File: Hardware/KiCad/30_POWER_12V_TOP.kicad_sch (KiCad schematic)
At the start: 0 parts

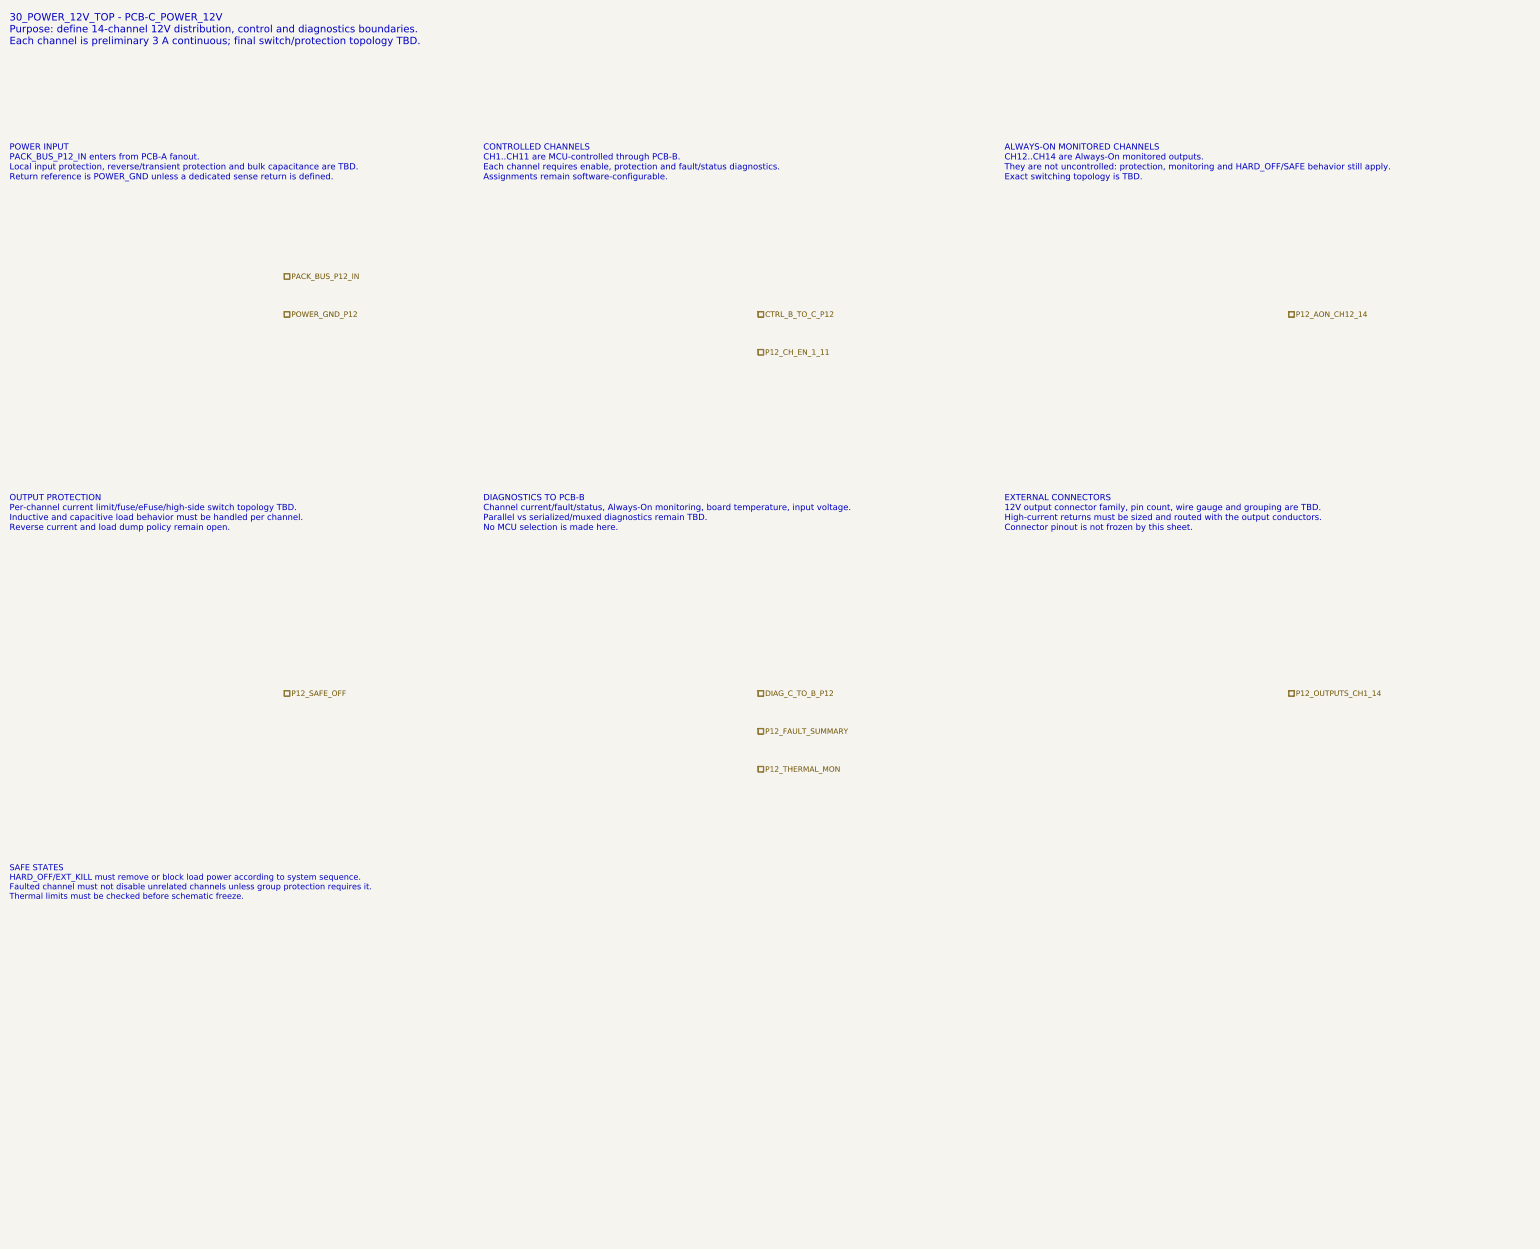
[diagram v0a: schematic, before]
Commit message: hardware: map PCB-C POWER_12V detailed hierarchy
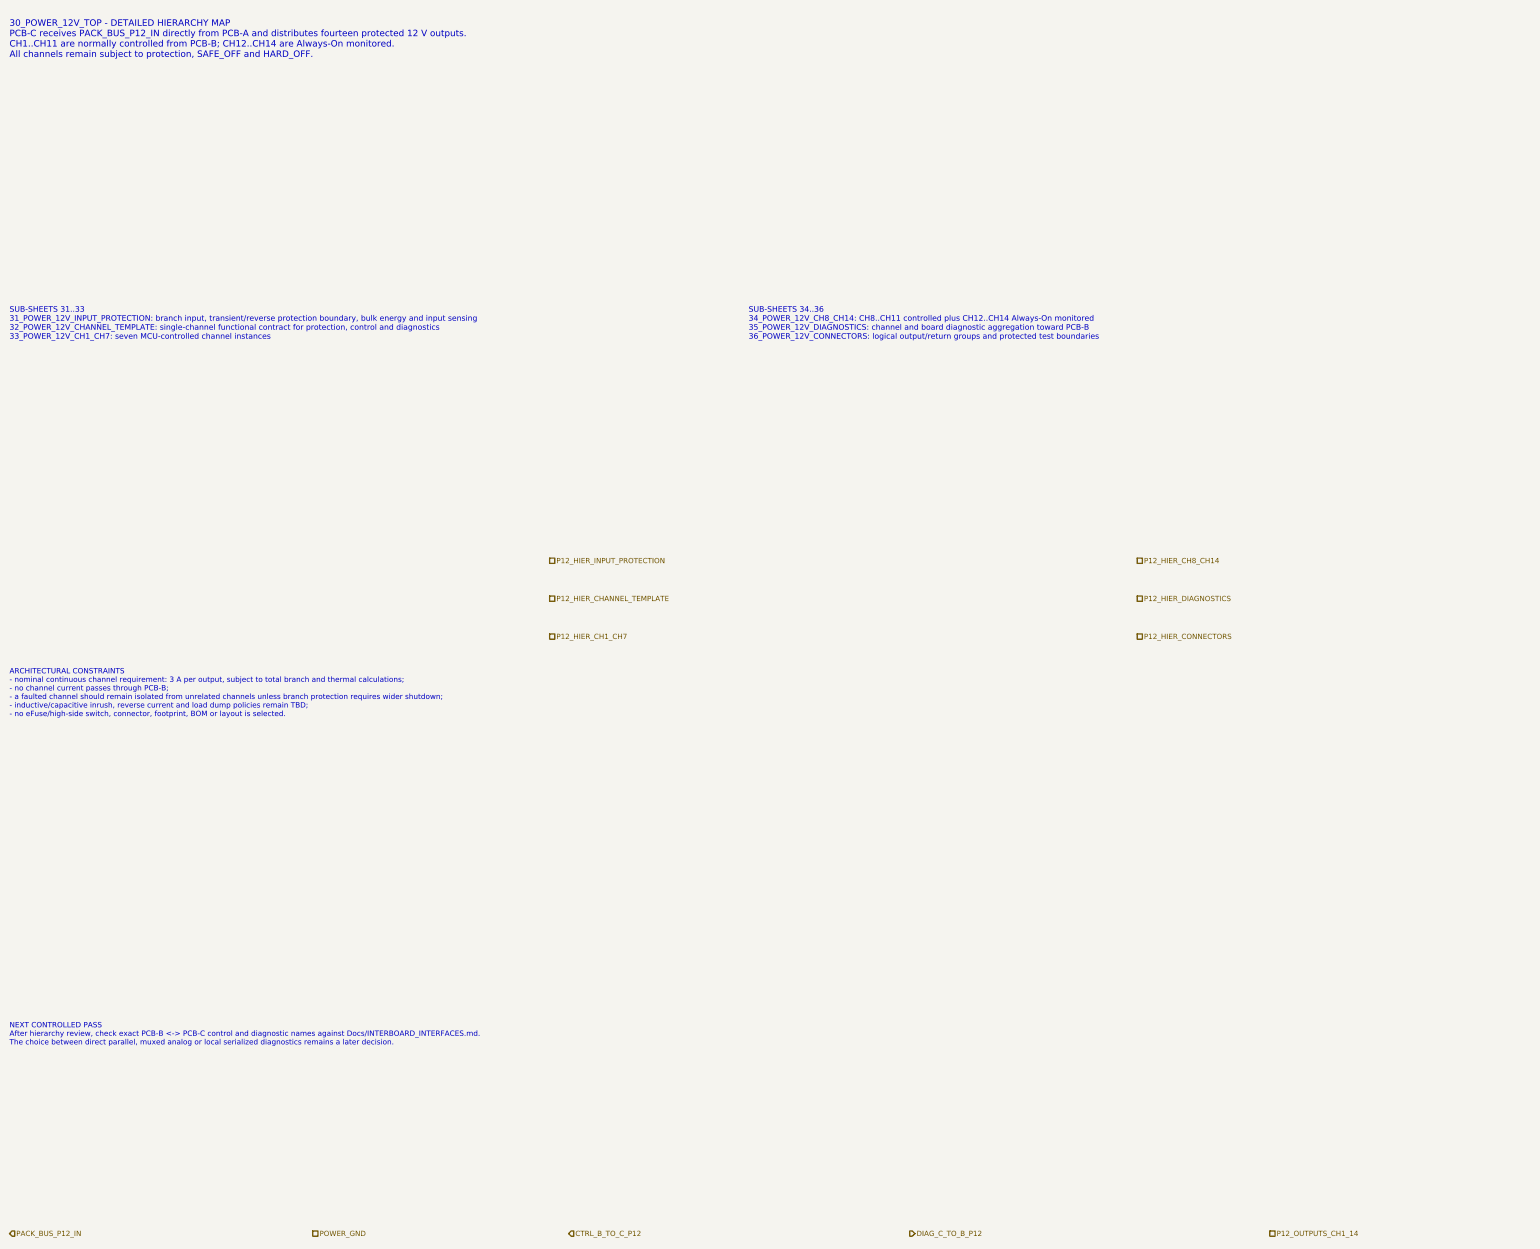
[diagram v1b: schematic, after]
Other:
- note added: "30_POWER_12V_TOP - DETAILED HIERARCHY MAP PCB-C receives PACK_BUS_P12_IN directly from PCB-A and distributes fourteen protected 12 V outputs. CH1..CH11 are normally controlled from PCB-B; CH12..CH14 are Always-On monitored. All channels remain subject to protection, SAFE_OFF and HARD_OFF."
- note added: "ARCHITECTURAL CONSTRAINTS - nominal continuous channel requirement: 3 A per output, subject to total branch and thermal calculations; - no channel current passes through PCB-B; - a faulted channel should remain isolated from unrelated channels unless branch protection requires wider shutdown; - inductive/capacitive inrush, reverse current and load dump policies remain TBD; - no eFuse/high-side sw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"
- note added: "NEXT CONTROLLED PASS After hierarchy review, check exact PCB-B <-> PCB-C control and diagnostic names against Docs/INTERBOARD_INTERFACES.md. The choice between direct parallel, muxed analog or local serialized diagnostics remains a later decision."
- note added: "SUB-SHEETS 31..33 31_POWER_12V_INPUT_PROTECTION: branch input, transient/reverse protection boundary, bulk energy and input sensing 32_POWER_12V_CHANNEL_TEMPLATE: single-channel functional contract for protection, control and diagnostics 33_POWER_12V_CH1_CH7: seven MCU-controlled channel instances"
- note added: "SUB-SHEETS 34..36 34_POWER_12V_CH8_CH14: CH8..CH11 controlled plus CH12..CH14 Always-On monitored 35_POWER_12V_DIAGNOSTICS: channel and board diagnostic aggregation toward PCB-B 36_POWER_12V_CONNECTORS: logical output/return groups and protected test boundaries"
- note removed: "30_POWER_12V_TOP - PCB-C_POWER_12V Purpose: define 14-channel 12V distribution, control and diagnostics boundaries. Each channel is preliminary 3 A continuous; final switch/protection topology TBD."
- note removed: "ALWAYS-ON MONITORED CHANNELS CH12..CH14 are Always-On monitored outputs. They are not uncontrolled: protection, monitoring and HARD_OFF/SAFE behavior still apply. Exact switching topology is TBD."
- note removed: "CONTROLLED CHANNELS CH1..CH11 are MCU-controlled through PCB-B. Each channel requires enable, protection and fault/status diagnostics. Assignments remain software-configurable."
- note removed: "DIAGNOSTICS TO PCB-B Channel current/fault/status, Always-On monitoring, board temperature, input voltage. Parallel vs serialized/muxed diagnostics remain TBD. No MCU selection is made here."
- note removed: "EXTERNAL CONNECTORS 12V output connector family, pin count, wire gauge and grouping are TBD. High-current returns must be sized and routed with the output conductors. Connector pinout is not frozen by this sheet."
- note removed: "OUTPUT PROTECTION Per-channel current limit/fuse/eFuse/high-side switch topology TBD. Inductive and capacitive load behavior must be handled per channel. Reverse current and load dump policy remain open."
- note removed: "POWER INPUT PACK_BUS_P12_IN enters from PCB-A fanout. Local input protection, reverse/transient protection and bulk capacitance are TBD. Return reference is POWER_GND unless a dedicated sense return is defined."
- note removed: "SAFE STATES HARD_OFF/EXT_KILL must remove or block load power according to system sequence. Faulted channel must not disable unrelated channels unless group protection requires it. Thermal limits must be checked before schematic freeze."
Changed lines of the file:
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@@
 		(title "30_POWER_12V_TOP - PCB-C_POWER_12V")
 		(date "2026-07-15")
-		(rev "A1")
+		(rev "A2")
 		(company "Gonoboben/plataVM")
-		(comment 1 "Architecture Level A: 14-channel 12V distribution")
-		(comment 2 "No eFuse/high-side switch part numbers or footprints selected")
+		(comment 1 "Architecture Level A/B: 14-channel POWER_12V detailed hierarchy map")
+		(comment 2 "Sub-sheets 31..36 define functional boundaries only; no components selected")
 	)
-	(text "30_POWER_12V_TOP - PCB-C_POWER_12V\nPurpose: define 14-channel 12V distribution, control and diagnostics boundaries.\nEach channel is preliminary 3 A continuous; final switch/protection topology TBD."
+	(text "30_POWER_12V_TOP - DETAILED HIERARCHY MAP\nPCB-C receives PACK_BUS_P12_IN directly from PCB-A and distributes fourteen protected 12 V outputs.\nCH1..CH11 are normally controlled from PCB-B; CH12..CH14 are Always-On monitored.\nAll channels remain subject to protection, SAFE_OFF and HARD_OFF."
 		(exclude_from_sim no)
-		(at 12 10 0)
-		(effects (font (size 1.55 1.55)) (justify left))
-		(uuid "p12-text-0001")
+		(at 12 12 0)
+		(effects (font (size 1.36 1.36)) (justify left))
+		(uuid "p12-top-00000030-0000-4000-8000-000000000101")
 	)
-	(text "POWER INPUT\nPACK_BUS_P12_IN enters from PCB-A fanout.\nLocal input protection, reverse/transient protection and bulk capacitance are TBD.\nReturn reference is POWER_GND unless a dedicated sense return is defined."
+	(text "SUB-SHEETS 31..33\n31_POWER_12V_INPUT_PROTECTION: branch input, transient/reverse protection boundary, bulk energy and input sensing\n32_POWER_12V_CHANNEL_TEMPLATE: single-channel functional contract for protection, control and diagnostics\n33_POWER_12V_CH1_CH7: seven MCU-controlled channel instances"
 		(exclude_from_sim no)
-		(at 12 38 0)
-		(effects (font (size 1.3 1.3)) (justify left))
-		(uuid "p12-text-0002")
+		(at 12 72 0)
+		(effects (font (size 1.18 1.18)) (justify left))
+		(uuid "p12-top-00000030-0000-4000-8000-000000000102")
 	)
-	(text "CONTROLLED CHANNELS\nCH1..CH11 are MCU-controlled through PCB-B.\nEach channel requires enable, protection and fault/status diagnostics.\nAssignments remain software-configurable."
+	(text "SUB-SHEETS 34..36\n34_POWER_12V_CH8_CH14: CH8..CH11 controlled plus CH12..CH14 Always-On monitored\n35_POWER_12V_DIAGNOSTICS: channel and board diagnostic aggregation toward PCB-B\n36_POWER_12V_CONNECTORS: logical output/return groups and protected test boundaries"
 		(exclude_from_sim no)
-		(at 112 38 0)
-		(effects (font (size 1.3 1.3)) (justify left))
-		(uuid "p12-text-0003")
+		(at 168 72 0)
+		(effects (font (size 1.18 1.18)) (justify left))
+		(uuid "p12-top-00000030-0000-4000-8000-000000000103")
 	)
-	(text "ALWAYS-ON MONITORED CHANNELS\nCH12..CH14 are Always-On monitored outputs.\nThey are not uncontrolled: protection, monitoring and HARD_OFF/SAFE behavior still apply.\nExact switching topology is TBD."
+	(text "ARCHITECTURAL CONSTRAINTS\n- nominal continuous channel requirement: 3 A per output, subject to total branch and thermal calculations;\n- no channel current passes through PCB-B;\n- a faulted channel should remain isolated from unrelated channels unless branch protection requires wider shutdown;\n- inductive/capacitive inrush, reverse current and load dump policies remain TBD;\n- no eFuse/high-side switch, connector, footprint, BOM or layout is selected."
 		(exclude_from_sim no)
-		(at 222 38 0)
-		(effects (font (size 1.3 1.3)) (justify left))
-		(uuid "p12-text-0004")
+		(at 12 150 0)
+		(effects (font (size 1.12 1.12)) (justify left))
+		(uuid "p12-top-00000030-0000-4000-8000-000000000104")
 	)
-	(text "OUTPUT PROTECTION\nPer-channel current limit/fuse/eFuse/high-side switch topology TBD.\nInductive and capacitive load behavior must be handled per channel.\nReverse current and load dump policy remain open."
+	(text "NEXT CONTROLLED PASS\nAfter hierarchy review, check exact PCB-B <-> PCB-C control and diagnostic names against Docs/INTERBOARD_INTERFACES.md.\nThe choice between direct parallel, muxed analog or local serialized diagnostics remains a later decision."
 		(exclude_from_sim no)
-		(at 12 112 0)
-		(effects (font (size 1.3 1.3)) (justify left))
-		(uuid "p12-text-0005")
+		(at 12 222 0)
+		(effects (font (size 1.12 1.12)) (justify left))
+		(uuid "p12-top-00000030-0000-4000-8000-000000000105")
 	)
-	(text "DIAGNOSTICS TO PCB-B\nChannel current/fault/status, Always-On monitoring, board temperature, input voltage.\nParallel vs serialized/muxed diagnostics remain TBD.\nNo MCU selection is made here."
-		(exclude_from_sim no)
-		(at 112 112 0)
-		(effects (font (size 1.3 1.3)) (justify left))
-		(uuid "p12-text-0006")
-	)
-	(text "EXTERNAL CONNECTORS\n12V output connector family, pin count, wire gauge and grouping are TBD.\nHigh-current returns must be sized and routed with the output conductors.\nConnector pinout is not frozen by this sheet."
-		(exclude_from_sim no)
-		(at 222 112 0)
-		(effects (font (size 1.3 1.3)) (justify left))
-		(uuid "p12-text-0007")
-	)
-	(text "SAFE STATES\nHARD_OFF/EXT_KILL must remove or block load power according to system sequence.\nFaulted channel must not disable unrelated channels unless group protection requires it.\nThermal limits must be checked before schematic freeze."
-		(exclude_from_sim no)
-		(at 12 190 0)
-		(effects (font (size 1.25 1.25)) (justify left))
-		(uuid "p12-text-0008")
-	)
-	(hierarchical_label "PACK_BUS_P12_IN" (shape passive) (exclude_from_sim no) (at 70 62 0) (effects (font (size 1.15 1.15)) (justify left)) (uuid "p12-label-0001"))
-	(hierarchical_label "POWER_GND_P12" (shape passive) (exclude_from_sim no) (at 70 70 0) (effects (font (size 1.15 1.15)) (justify left)) (uuid "p12-label-0002"))
-	(hierarchical_label "CTRL_B_TO_C_P12" (shape passive) (exclude_from_sim no) (at 170 70 0) (effects (font (size 1.15 1.15)) (justify left)) (uuid "p12-label-0003"))
-	(hierarchical_label "P12_CH_EN_1_11" (shape passive) (exclude_from_sim no) (at 170 78 0) (effects (font (size 1.15 1.15)) (justify left)) (uuid "p12-label-0004"))
-	(hierarchical_label "P12_AON_CH12_14" (shape passive) (exclude_from_sim no) (at 282 70 0) (effects (font (size 1.15 1.15)) (justify left)) (uuid "p12-label-0005"))
-	(hierarchical_label "P12_OUTPUTS_CH1_14" (shape passive) (exclude_from_sim no) (at 282 150 0) (effects (font (size 1.15 1.15)) (justify left)) (uuid "p12-label-0006"))
-	(hierarchical_label "DIAG_C_TO_B_P12" (shape passive) (exclude_from_sim no) (at 170 150 0) (effects (font (size 1.15 1.15)) (justify left)) (uuid "p12-label-0007"))
-	(hierarchical_label "P12_FAULT_SUMMARY" (shape passive) (exclude_from_sim no) (at 170 158 0) (effects (font (size 1.15 1.15)) (justify left)) (uuid "p12-label-0008"))
-	(hierarchical_label "P12_SAFE_OFF" (shape passive) (exclude_from_sim no) (at 70 150 0) (effects (font (size 1.15 1.15)) (justify left)) (uuid "p12-label-0009"))
-	(hierarchical_label "P12_THERMAL_MON" (shape passive) (exclude_from_sim no) (at 170 166 0) (effects (font (size 1.15 1.15)) (justify left)) (uuid "p12-label-0010"))
+	(hierarchical_label "P12_HIER_INPUT_PROTECTION" (shape passive) (exclude_from_sim no) (at 126 122 0) (effects (font (size 1.1 1.1)) (justify left)) (uuid "p12-top-00000030-0000-4000-8000-000000000201"))
+	(hierarchical_label "P12_HIER_CHANNEL_TEMPLATE" (shape passive) (exclude_from_sim no) (at 126 130 0) (effects (font (size 1.1 1.1)) (justify left)) (uuid "p12-top-00000030-0000-4000-8000-000000000202"))
+	(hierarchical_label "P12_HIER_CH1_CH7" (shape passive) (exclude_from_sim no) (at 126 138 0) (effects (font (size 1.1 1.1)) (justify left)) (uuid "p12-top-00000030-0000-4000-8000-000000000203"))
+	(hierarchical_label "P12_HIER_CH8_CH14" (shape passive) (exclude_from_sim no) (at 250 122 0) (effects (font (size 1.1 1.1)) (justify left)) (uuid "p12-top-00000030-0000-4000-8000-000000000204"))
+	(hierarchical_label "P12_HIER_DIAGNOSTICS" (shape passive) (exclude_from_sim no) (at 250 130 0) (effects (font (size 1.1 1.1)) (justify left)) (uuid "p12-top-00000030-0000-4000-8000-000000000205"))
+	(hierarchical_label "P12_HIER_CONNECTORS" (shape passive) (exclude_from_sim no) (at 250 138 0) (effects (font (size 1.1 1.1)) (justify left)) (uuid "p12-top-00000030-0000-4000-8000-000000000206"))
+	(hierarchical_label "PACK_BUS_P12_IN" (shape input) (exclude_from_sim no) (at 12 264 0) (effects (font (size 1.1 1.1)) (justify left)) (uuid "p12-top-00000030-0000-4000-8000-000000000207"))
+	(hierarchical_label "POWER_GND" (shape passive) (exclude_from_sim no) (at 76 264 0) (effects (font (size 1.1 1.1)) (justify left)) (uuid "p12-top-00000030-0000-4000-8000-000000000208"))
+	(hierarchical_label "CTRL_B_TO_C_P12" (shape input) (exclude_from_sim no) (at 130 264 0) (effects (font (size 1.1 1.1)) (justify left)) (uuid "p12-top-00000030-0000-4000-8000-000000000209"))
+	(hierarchical_label "DIAG_C_TO_B_P12" (shape output) (exclude_from_sim no) (at 202 264 0) (effects (font (size 1.1 1.1)) (justify left)) (uuid "p12-top-00000030-0000-4000-8000-000000000210"))
+	(hierarchical_label "P12_OUTPUTS_CH1_14" (shape passive) (exclude_from_sim no) (at 278 264 0) (effects (font (size 1.1 1.1)) (justify left)) (uuid "p12-top-00000030-0000-4000-8000-000000000211"))
 )
